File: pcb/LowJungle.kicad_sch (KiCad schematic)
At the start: 0 parts

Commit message: Finished schematic
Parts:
- added H1, H2, H3, H4, H5, H6, H7: MountingHole_Pad, MountingHole:MountingHole_3.2mm_M3_DIN965_Pad_TopOnly, symbol Mechanical:MountingHole_Pad
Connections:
- new net GND: H1.1, H2.1, H3.1, H4.1, H5.1, H6.1, H7.1
- no-connect marks 0 -> 1
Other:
- added sheet Bits (bits.kicad_sch)
- added sheet MCU (mcu.kicad_sch)
- added sheet USB (usb.kicad_sch)

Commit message: Started routing
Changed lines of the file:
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@@
 	)
 	(sheet
-		(at 161.29 49.53)
-		(size 26.67 54.61)
+		(at 161.29 41.91)
+		(size 26.67 62.23)
 		(exclude_from_sim no)
 		(in_bom yes)
@@
 		)
 		(property "Sheetname" "KeyMatrix"
-			(at 161.29 48.8184 0)
+			(at 161.29 41.1984 0)
 			(effects
 				(font
@@
 			)
 		)
-		(pin "GPIO_1" input
+		(pin "GPIO_1" output
 			(at 135.89 138.43 0)
 			(effects

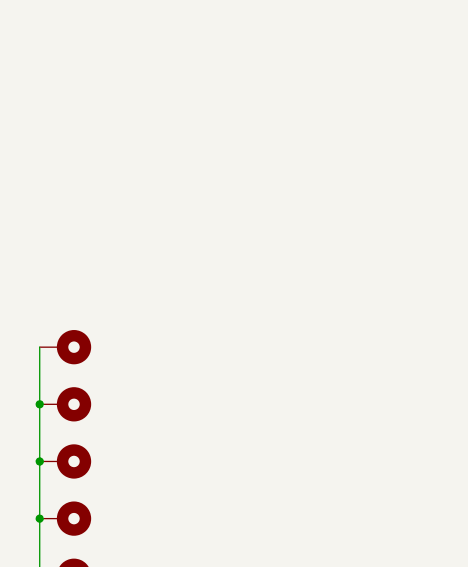
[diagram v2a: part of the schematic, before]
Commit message: added more mounting holes
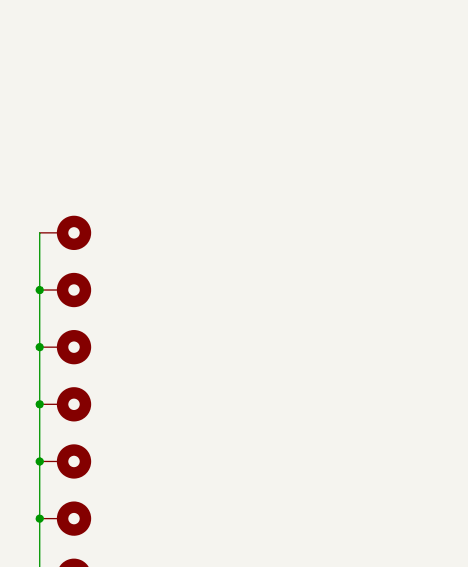
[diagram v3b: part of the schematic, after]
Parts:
- added H8, H9: MountingHole_Pad, MountingHole:MountingHole_3.2mm_M3_DIN965_Pad_TopOnly, symbol Mechanical:MountingHole_Pad
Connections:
- net GND: now also H8.1, H9.1
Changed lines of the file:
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@@
+	)
+	(junction
+		(at 41.91 116.84)
+		(diameter 0)
+		(color 0 0 0 0)
+	)
+	(junction
+		(at 41.91 123.19)
+		(diameter 0)
+		(color 0 0 0 0)
 	)
 	(junction
@@
 	(wire
 		(pts
+			(xy 41.91 116.84) (xy 41.91 123.19)
+		)
+		(stroke
+			(width 0)
+			(type default)
+		)
+	)
+	(wire
+		(pts
 			(xy 135.89 95.25) (xy 161.29 95.25)
 		)
@@
 		(pts
 			(xy 135.89 97.79) (xy 161.29 97.79)
+		)
+		(stroke
+			(width 0)
+			(type default)
+		)
+	)
+	(wire
+		(pts
+			(xy 41.91 110.49) (xy 41.91 116.84)
 		)
 		(stroke
@@
 	(symbol
 		(lib_id "Mechanical:MountingHole_Pad")
+		(at 44.45 116.84 270)
+		(unit 1)
+		(exclude_from_sim yes)
+		(in_bom no)
+		(on_board yes)
+		(dnp no)
+		(fields_autoplaced yes)
+		(property "Reference" "H8"
+			(at 48.26 115.5699 90)
+			(effects
+				(font
+					(size 1.27 1.27)
+				)
+				(justify left)
+				(hide yes)
+			)
+		)
+		(property "Value" "MountingHole_Pad"
+			(at 48.26 118.1099 90)
+			(effects
+				(font
+					(size 1.27 1.27)
+				)
+				(justify left)
+				(hide yes)
+			)
+		)
+		(property "Footprint" "MountingHole:MountingHole_3.2mm_M3_DIN965_Pad_TopOnly"
+			(at 44.45 116.84 0)
+			(effects
+				(font
+					(size 1.27 1.27)
+				)
+				(hide yes)
+			)
+		)
+		(property "Datasheet" "~"
+			(at 44.45 116.84 0)
+			(effects
+				(font
+					(size 1.27 1.27)
+				)
+				(hide yes)
+			)
+		)
+		(property "Description" "Mounting Hole with connection"
+			(at 44.45 116.84 0)
+			(effects
+				(font
+					(size 1.27 1.27)
+				)
+				(hide yes)
+			)
+		)
+		(pin "1"
+		)
+		(instances
+			(project "LowJungle"
+				(path "/35a333ff-4765-4a57-b568-da2531002cc6"
+					(reference "H8")
+					(unit 1)
+				)
+			)
+		)
+	)
+	(symbol
+		(lib_id "Mechanical:MountingHole_Pad")
 		(at 44.45 154.94 270)
 		(unit 1)
@@
 					(unit 1)
 				)
+			)
+		)
+	)
+	(symbol
+		(lib_id "Mechanical:MountingHole_Pad")
+		(at 44.45 110.49 270)
+		(unit 1)
+		(exclude_from_sim yes)
+		(in_bom no)
+		(on_board yes)
+		(dnp no)
+		(fields_autoplaced yes)
+		(property "Reference" "H9"
+			(at 48.26 109.2199 90)
+			(effects
+				(font
+					(size 1.27 1.27)
+				)
+				(justify left)
+				(hide yes)
+			)
+		)
+		(property "Value" "MountingHole_Pad"
+			(at 48.26 111.7599 90)
+			(effects
+				(font
+					(size 1.27 1.27)
+				)
+				(justify left)
+				(hide yes)
+			)
+		)
+		(property "Footprint" "MountingHole:MountingHole_3.2mm_M3_DIN965_Pad_TopOnly"
+			(at 44.45 110.49 0)
+			(effects
+				(font
+					(size 1.27 1.27)
+				)
+				(hide yes)
+			)
+		)
+		(property "Datasheet" "~"
+			(at 44.45 110.49 0)
+			(effects
+				(font
+					(size 1.27 1.27)
+				)
+				(hide yes)
+			)
+		)
+		(property "Description" "Mounting Hole with connection"
+			(at 44.45 110.49 0)
+			(effects
+				(font
+					(size 1.27 1.27)
+				)
+				(hide yes)
+			)
+		)
+		(pin "1"
+		)
+		(instances
+			(project "LowJungle"
+				(path "/35a333ff-4765-4a57-b568-da2531002cc6"
+					(reference "H9")
+					(unit 1)
+				)
